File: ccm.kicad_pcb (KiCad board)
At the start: 2 copper layers, 80.1 x 75.2 mm, 25 parts, among them J1 Conn_01x06_Socket, J2 Conn_01x06_Socket, J3 Conn_01x04_Socket, J4 Conn_01x04_Socket, J5 Conn_01x04_Socket, J6 Conn_01x02_Socket, J7 Conn_01x02_Socket, U1 Teensy4.1, U2 LM1117DT-1.8, U3 SN65HVD230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

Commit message: add bottom gnd zone
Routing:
- added copper zone on B.Cu, net GLV-
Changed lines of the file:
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@@
 			(thermal_bridge_angle 45)
 		)
+		(model "${KICAD8_3DMODEL_DIR}/Resistor_SMD.3dshapes/R_0805_2012Metric.wrl"
+			(offset
+				(xyz 1.25 0 0)
+			)
+			(scale
+				(xyz 1 1 1)
+			)
+			(rotate
+				(xyz 0 0 0)
+			)
+		)
+		(model "${KICAD8_3DMODEL_DIR}/Resistor_SMD.3dshapes/R_0805_2012Metric.wrl"
+			(offset
+				(xyz -1.25 0 0)
+			)
+			(scale
+				(xyz 1 1 1)
+			)
+			(rotate
+				(xyz 0 0 0)
+			)
+		)
 	)
 	(footprint "Package_SO:SOIC-8_3.9x4.9mm_P1.27mm"
@@
 			(thermal_bridge_angle 45)
 		)
+		(model "${KICAD8_3DMODEL_DIR}/Resistor_SMD.3dshapes/R_0805_2012Metric.wrl"
+			(offset
+				(xyz 1.25 0 0)
+			)
+			(scale
+				(xyz 1 1 1)
+			)
+			(rotate
+				(xyz 0 0 0)
+			)
+		)
+		(model "${KICAD8_3DMODEL_DIR}/Resistor_SMD.3dshapes/R_0805_2012Metric.wrl"
+			(offset
+				(xyz -1.25 0 0)
+			)
+			(scale
+				(xyz 1 1 1)
+			)
+			(rotate
+				(xyz 0 0 0)
+			)
+		)
 	)
 	(footprint "voltagedivider:Voltage_Divider"
@@
 			(thermal_bridge_angle 45)
 		)
+		(model "${KICAD8_3DMODEL_DIR}/Resistor_SMD.3dshapes/R_0805_2012Metric.wrl"
+			(offset
+				(xyz 1.25 0 0)
+			)
+			(scale
+				(xyz 1 1 1)
+			)
+			(rotate
+				(xyz 0 0 0)
+			)
+		)
+		(model "${KICAD8_3DMODEL_DIR}/Resistor_SMD.3dshapes/R_0805_2012Metric.wrl"
+			(offset
+				(xyz -1.25 0 0)
+			)
+			(scale
+				(xyz 1 1 1)
+			)
+			(rotate
+				(xyz 0 0 0)
+			)
+		)
 	)
 	(footprint "Resistor_SMD:R_0805_2012Metric_Pad1.20x1.40mm_HandSolder"
@@
 			(thermal_bridge_angle 45)
 		)
+		(model "${KICAD8_3DMODEL_DIR}/Resistor_SMD.3dshapes/R_0805_2012Metric.wrl"
+			(offset
+				(xyz 1.25 0 0)
+			)
+			(scale
+				(xyz 1 1 1)
+			)
+			(rotate
+				(xyz 0 0 0)
+			)
+		)
+		(model "${KICAD8_3DMODEL_DIR}/Resistor_SMD.3dshapes/R_0805_2012Metric.wrl"
+			(offset
+				(xyz -1.25 0 0)
+			)
+			(scale
+				(xyz 1 1 1)
+			)
+			(rotate
+				(xyz 0 0 0)
+			)
+		)
 	)
 	(footprint "voltagedivider:Voltage_Divider"
@@
 			(thermal_bridge_angle 45)
 		)
+		(model "${KICAD8_3DMODEL_DIR}/Resistor_SMD.3dshapes/R_0805_2012Metric.wrl"
+			(offset
+				(xyz 1.25 0 0)
+			)
+			(scale
+				(xyz 1 1 1)
+			)
+			(rotate
+				(xyz 0 0 0)
+			)
+		)
+		(model "${KICAD8_3DMODEL_DIR}/Resistor_SMD.3dshapes/R_0805_2012Metric.wrl"
+			(offset
+				(xyz -1.25 0 0)
+			)
+			(scale
+				(xyz 1 1 1)
+			)
+			(rotate
+				(xyz 0 0 0)
+			)
+		)
 	)
 	(footprint "Package_SO:SOIC-8_3.9x4.9mm_P1.27mm"
@@
 			(thermal_bridge_angle 45)
 		)
+		(model "${KICAD8_3DMODEL_DIR}/Resistor_SMD.3dshapes/R_0805_2012Metric.wrl"
+			(offset
+				(xyz 1.25 0 0)
+			)
+			(scale
+				(xyz 1 1 1)
+			)
+			(rotate
+				(xyz 0 0 0)
+			)
+		)
+		(model "${KICAD8_3DMODEL_DIR}/Resistor_SMD.3dshapes/R_0805_2012Metric.wrl"
+			(offset
+				(xyz -1.25 0 0)
+			)
+			(scale
+				(xyz 1 1 1)
+			)
+			(rotate
+				(xyz 0 0 0)
+			)
+		)
 	)
 	(footprint "Connector_Molex:Molex_Mini-Fit_Jr_5566-02A2_2x01_P4.20mm_Vertical"
@@
 			(thermal_bridge_angle 45)
 		)
+		(model "${KICAD8_3DMODEL_DIR}/Resistor_SMD.3dshapes/R_0805_2012Metric.wrl"
+			(offset
+				(xyz 1.25 0 0)
+			)
+			(scale
+				(xyz 1 1 1)
+			)
+			(rotate
+				(xyz 0 0 0)
+			)
+		)
+		(model "${KICAD8_3DMODEL_DIR}/Resistor_SMD.3dshapes/R_0805_2012Metric.wrl"
+			(offset
+				(xyz -1.25 0 0)
+			)
+			(scale
+				(xyz 1 1 1)
+			)
+			(rotate
+				(xyz 0 0 0)
+			)
+		)
 	)
 	(footprint "Connector_Molex:Molex_Mini-Fit_Jr_5566-04A2_2x02_P4.20mm_Vertical"
@@
 			(thermal_bridge_angle 45)
 		)
+		(model "${KICAD8_3DMODEL_DIR}/Resistor_SMD.3dshapes/R_0805_2012Metric.wrl"
+			(offset
+				(xyz 1.25 0 0)
+			)
+			(scale
+				(xyz 1 1 1)
+			)
+			(rotate
+				(xyz 0 0 0)
+			)
+		)
+		(model "${KICAD8_3DMODEL_DIR}/Resistor_SMD.3dshapes/R_0805_2012Metric.wrl"
+			(offset
+				(xyz -1.25 0 0)
+			)
+			(scale
+				(xyz 1 1 1)
+			)
+			(rotate
+				(xyz 0 0 0)
+			)
+		)
 	)
 	(gr_line
@@
 	)
 	(gr_text "Central Computer \nModule v1"
-		(at 144.5 135.5 0)
+		(at 156.25 134.95 0)
 		(layer "F.SilkS")
 		(effects
@@
 		(net 60)
 	)
+	(zone
+		(net 2)
+		(net_name "GLV-")
+		(layer "B.Cu")
+		(hatch edge 0.5)
+		(connect_pads
+			(clearance 0.5)
+		)
+		(min_thickness 0.25)
+		(filled_areas_thickness no)
+		(fill yes
+			(thermal_gap 0.5)
+			(thermal_bridge_width 0.5)
+		)
+		(polygon
+			(pts
+				(xy 109 59.5) (xy 189 59.5) (xy 189 137) (xy 109 137)
+			)
+		)
+	)
 )

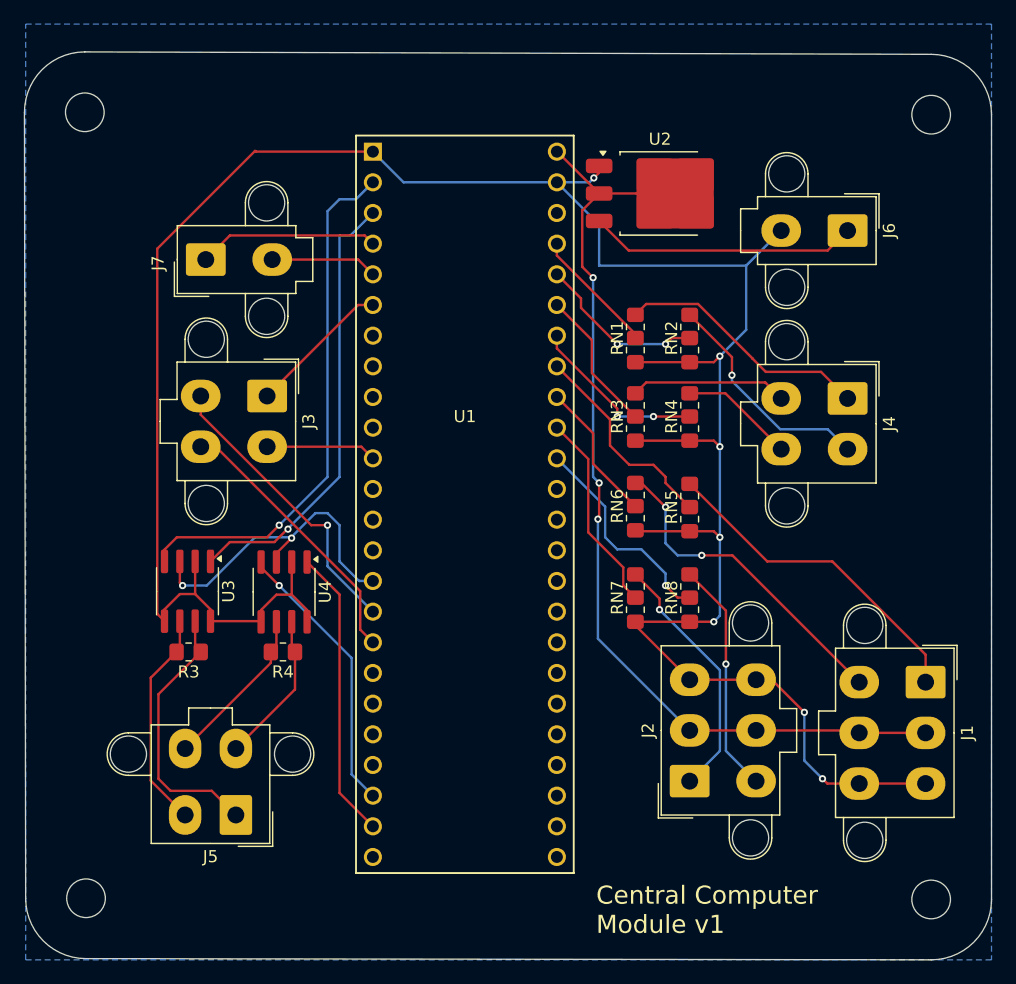
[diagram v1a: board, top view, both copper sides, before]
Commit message: thicken power trace widths
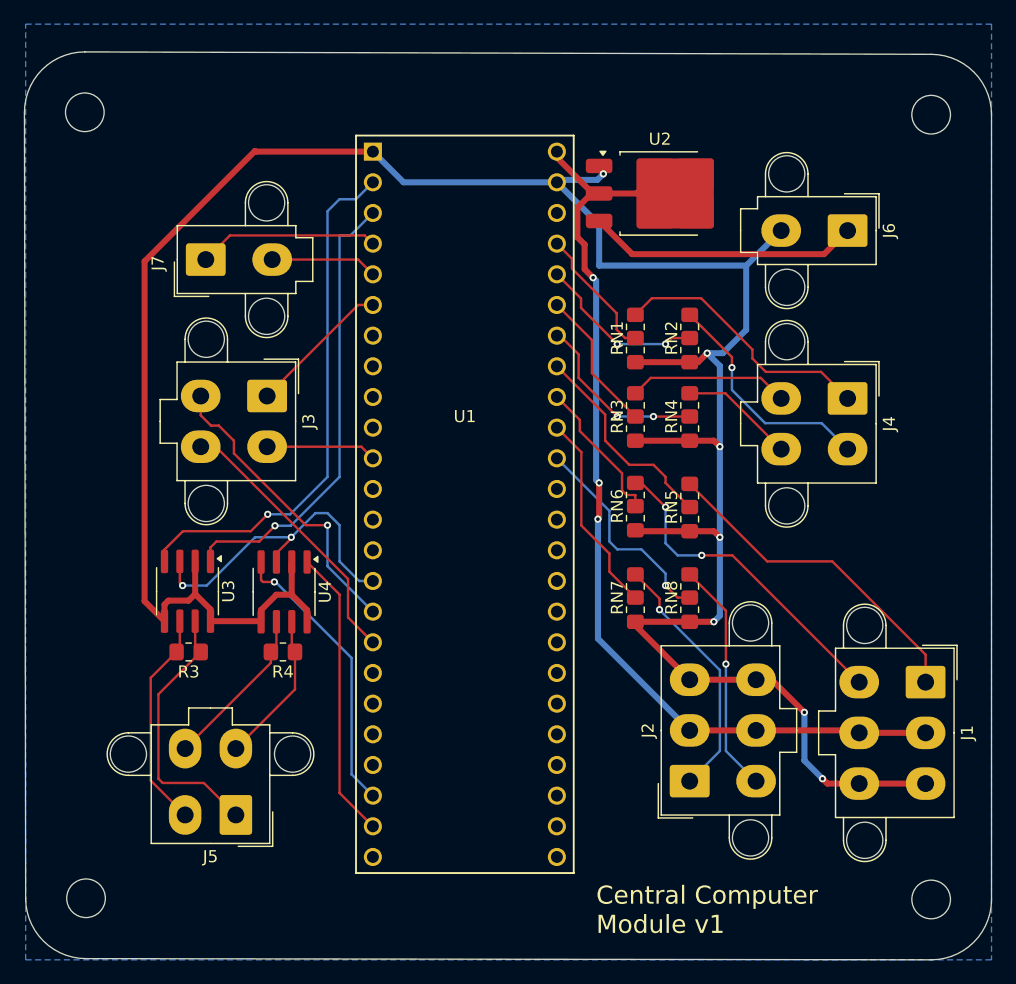
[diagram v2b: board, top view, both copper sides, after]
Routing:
- net GLV-: track 211.7 -> 214.1 mm
- net +5V: track 78.6 -> 79.6 mm
- net Net-(U1-23_A9_CRX1_MCLK1): track 10.5 -> 11.3 mm
- net lin_pot_1: track 21.2 -> 22.0 mm
- net i2c_SCL: track 24.6 -> 25.2 mm
- net CAN_RX_2: track 23.2 -> 23.8 mm
- net CAN_TX_1: track 37.2 -> 37.8 mm

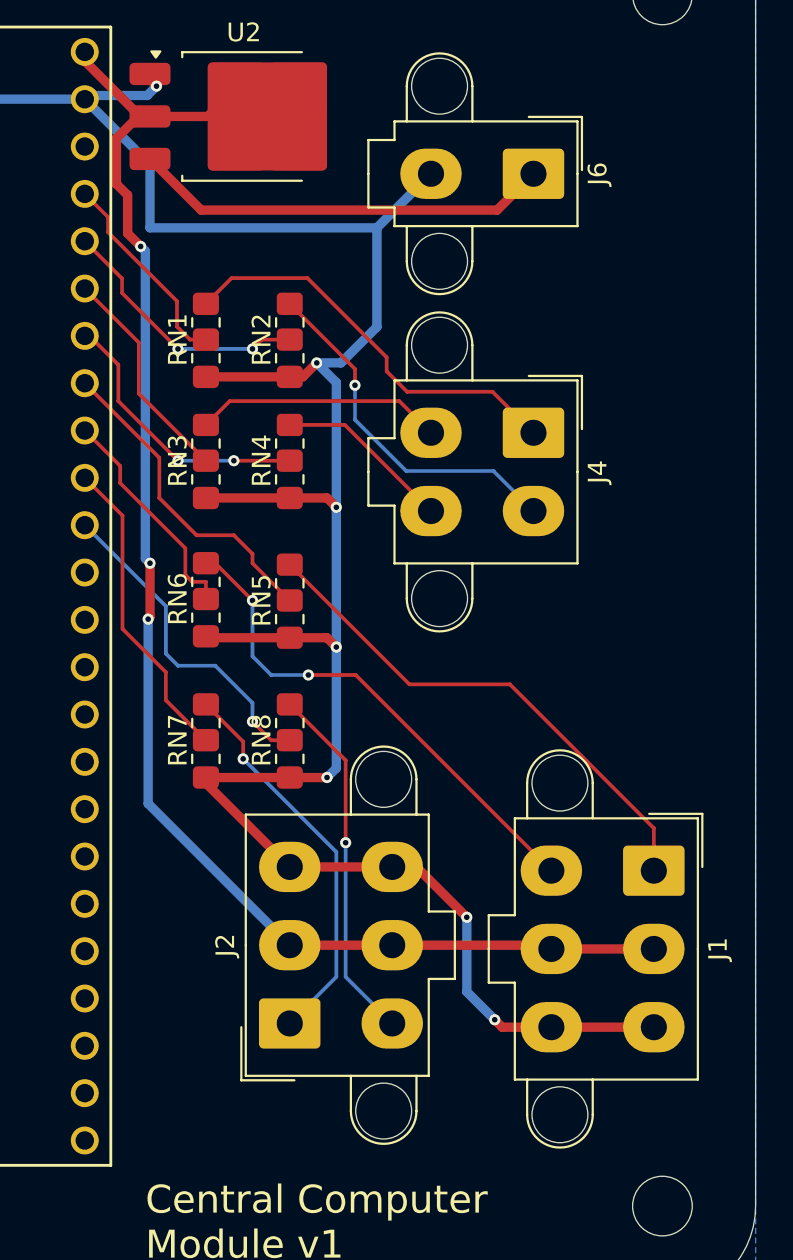
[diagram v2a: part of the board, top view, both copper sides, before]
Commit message: remove 5v/glv from throttle/brake sensors
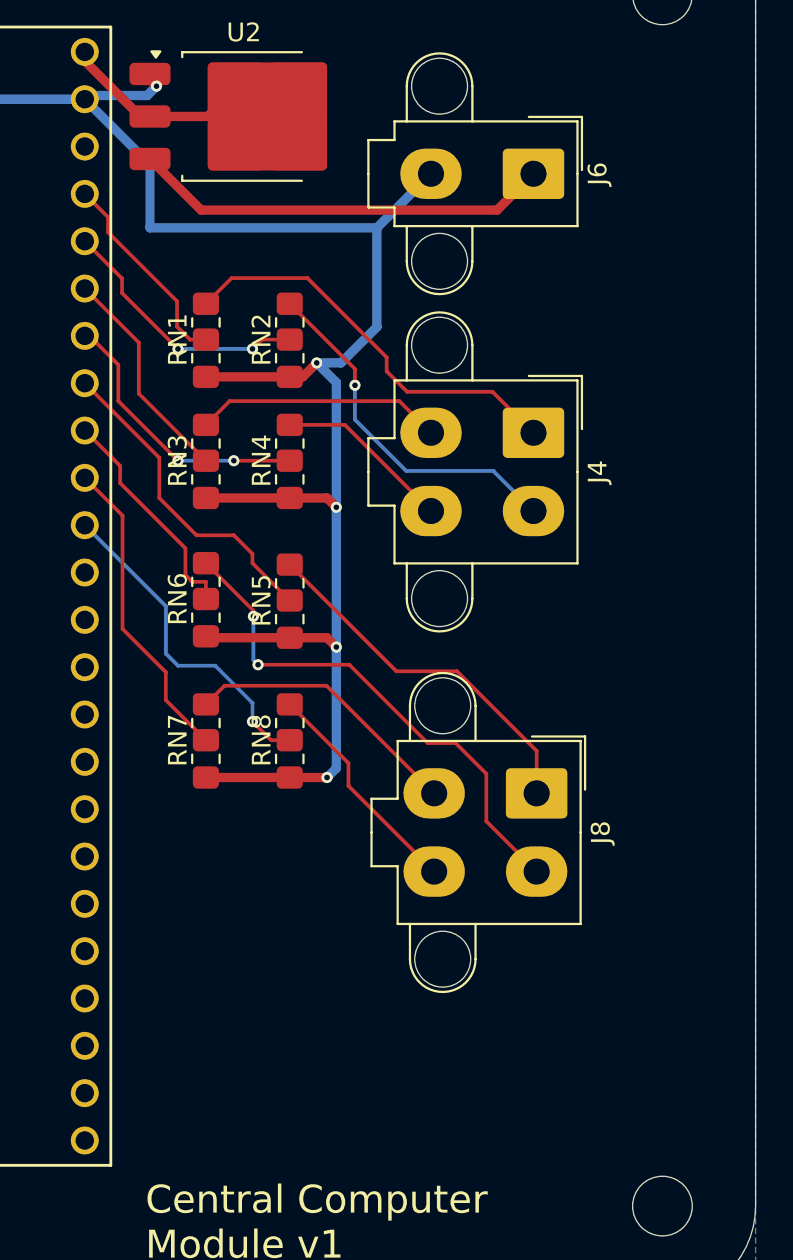
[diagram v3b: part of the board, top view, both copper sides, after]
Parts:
- removed J1, J2: Conn_01x06_Socket, Connector_Molex:Molex_Mini-Fit_Jr_5566-06A2_2x03_P4.20mm_Vertical
- added J8: Conn_01x04_Socket, Connector_Molex:Molex_Mini-Fit_Jr_5566-04A2_2x02_P4.20mm_Vertical, F.Cu at (177.2, 109.8)
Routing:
- net +5V: track 79.6 -> 11.1 mm, vias 3 -> 0
- net GLV-: track 214.1 -> 181.9 mm, vias 7 -> 5
- net acc_ped_1: track 27.7 -> 19.7 mm
- net brake_2: track 19.4 -> 12.2 mm, vias 1 -> 0
- net brake_1: track 21.1 -> 15.1 mm, vias 1 -> 0
- net acc_ped_2: track 27.1 -> 27.7 mm
